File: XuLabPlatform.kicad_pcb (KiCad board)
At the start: 2 copper layers, 134 x 123.5 mm, 73 parts, among them J1 SWD Connector, J10 Servo7, J11 Servo8, J12 Thruster SGN, J13 USB_B_Micro, J14 CAN, J15 I2C, J16 UART, J2 Conn_01x04, J3 1986660-2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

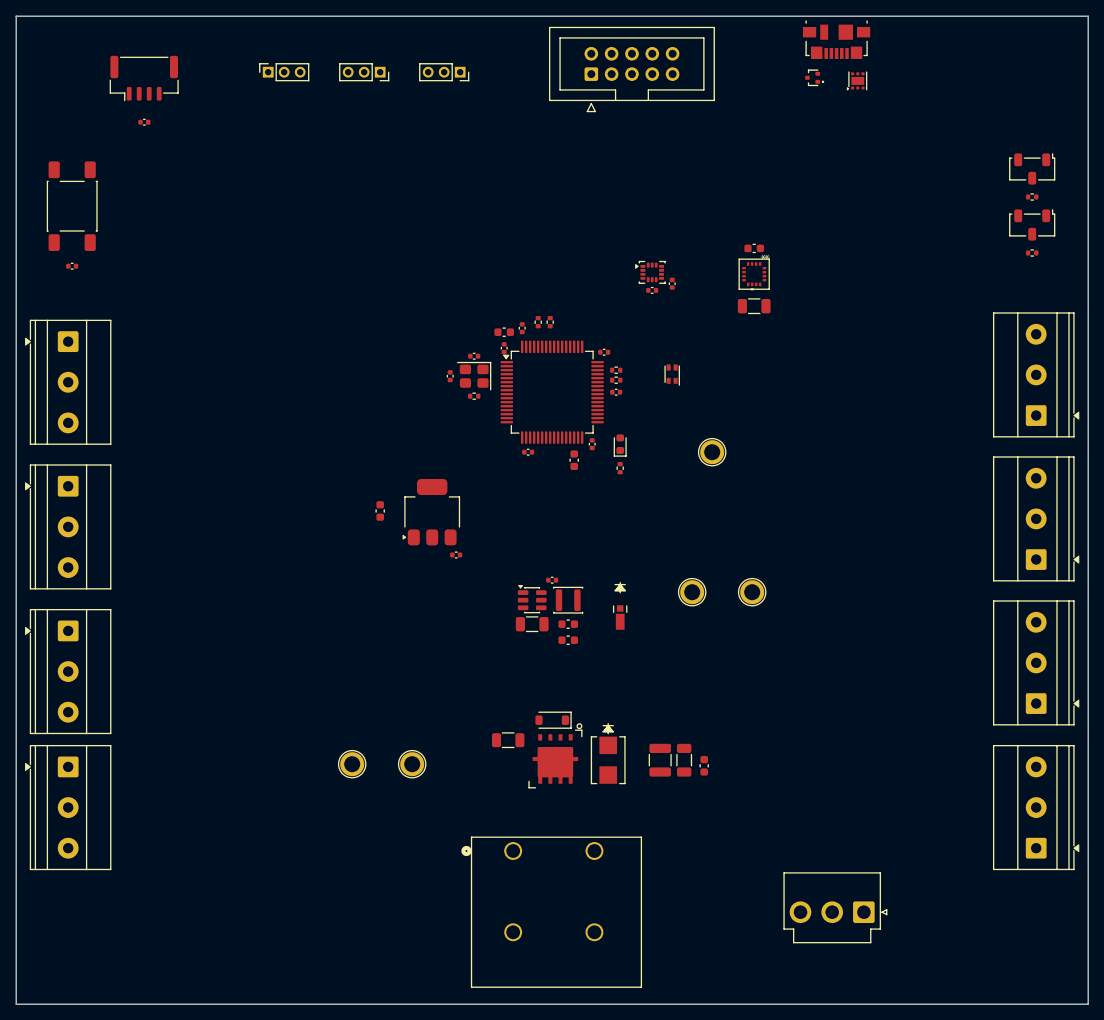
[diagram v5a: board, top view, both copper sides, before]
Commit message: Add ground plane and crystal connections
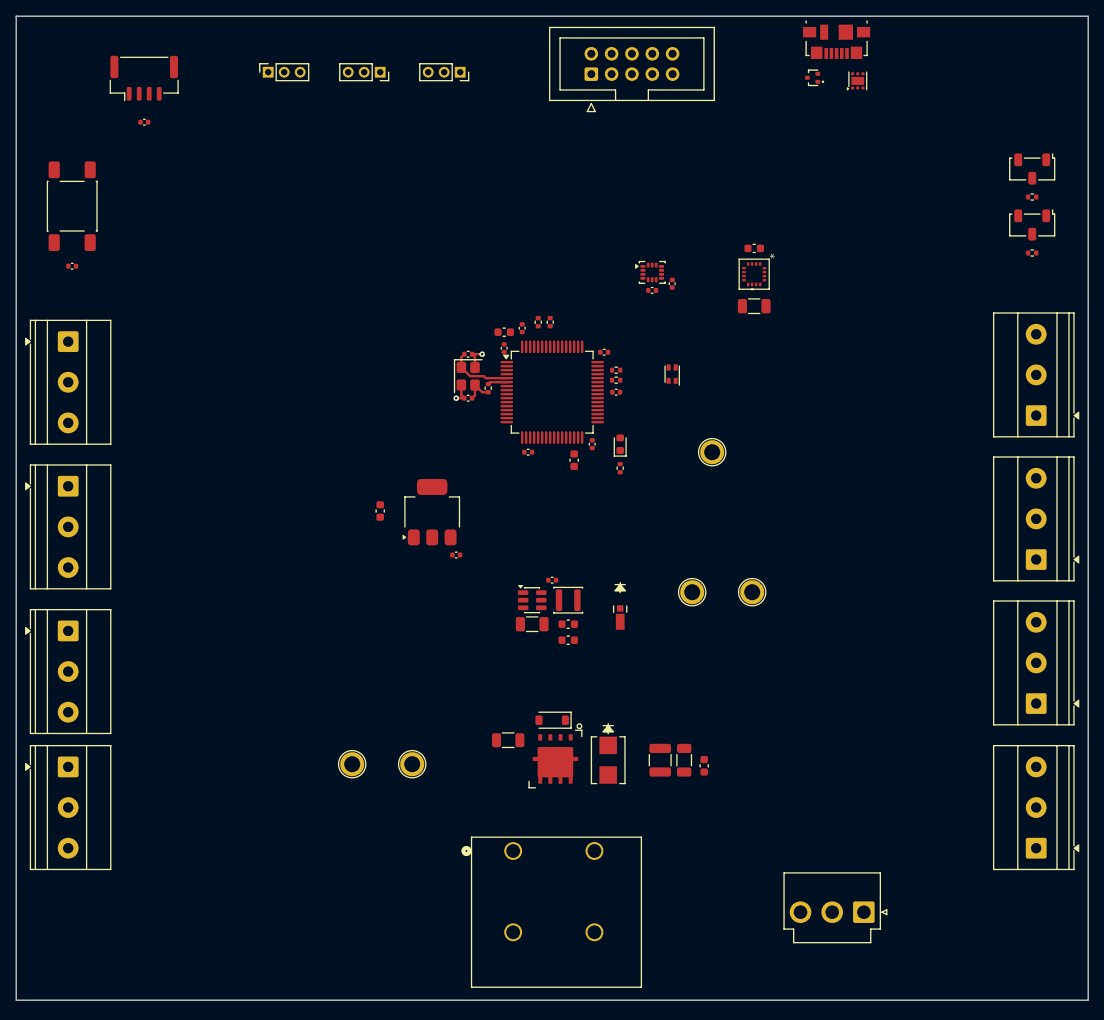
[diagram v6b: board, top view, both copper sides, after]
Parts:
- moved C12 3.55 mm to (139.5, 80.8), turned to 180 degrees
- moved R3 2.02 mm to (142.0, 79.5), turned to -90 degrees
- moved C11 0.79 mm to (139.5, 75.2), turned to 0 degrees
- moved Y1 0.75 mm to (139.5, 78.0), turned to -90 degrees
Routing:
- net /MCU A/RCC_IN: track 0.00 -> 8.04 mm
- net GND: track 0.00 -> 7.15 mm, vias 0 -> 2
- net Net-(C12-Pad1): track 0.00 -> 3.83 mm
- net /MCU A/RCC_OUT: track 0.00 -> 2.42 mm
- added copper zone on In1.Cu, net GND
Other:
- board size 134 x 123.5 mm -> 134 x 123 mm
- copper layers 2 -> 4

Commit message: Add rest of connections
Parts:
- C7, C8, U6: moved to B.Cu
- D2: value 4.7V -> 12V
- R9: value 75 -> 100
- moved SW3 104.5 mm to (105.5, 59.8)
- moved SW2 104.5 mm to (105.5, 52.1)
- moved R1 104.0 mm to (106.0, 55.2)
- moved R2 104.0 mm to (106.0, 62.8)
- moved J12 80.3 mm to (200.2, 65.5), turned to 90 degrees
- moved J4 54.9 mm to (99.5, 72.8)
- moved J7 54.1 mm to (99.5, 126.8)
- moved SW1 40.0 mm to (124.2, 77.5), turned to 180 degrees
- moved C10 30.5 mm to (117.5, 77.5), turned to 90 degrees
- moved J5 21.5 mm to (99.5, 90.8)
- moved J6 19.8 mm to (99.5, 108.8)
- moved R5 17.7 mm to (135.5, 59.0)
- moved R4 17.0 mm to (138.0, 59.0)
- moved CR2 14.5 mm to (144.1, 106.2)
- moved C8 13.8 mm to (142.1, 92.8)
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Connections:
- C13 pad 1: +3V3 -> +3.3V
- C14 pad 1: +3V3 -> +3.3V
- C15 pad 1: +3V3 -> +3.3V
- C17 pad 1: +3V3 -> +3.3V
- D3 pad 1: /MCU A/USB_D_I+ -> /MCU A/USB_D_I-
- D3 pad 2: /MCU A/USB_D_I- -> /MCU A/USB_D_I+
- J10 pad 1: /PWM_7 -> GND
- J10 pad 3: GND -> /PWM_7
- J11 pad 1: /PWM_8 -> GND
- J11 pad 3: GND -> /PWM_8
- J12 pad 1: /PWM_9 -> GND
- J12 pad 3: GND -> /PWM_9
- J15 pad 1: /I2C1_SCL -> /I2C1_SDA
- J15 pad 2: /I2C1_SDA -> /I2C1_SCL
- J16 pad 1: /UART_TX -> /UART_RX
- J16 pad 2: /UART_RX -> /UART_TX
- J2 pad 1: +3V3 -> +3.3V
- J8 pad 1: /PWM_5 -> GND
- J8 pad 3: GND -> /PWM_5
- J9 pad 1: /PWM_6 -> GND
- J9 pad 3: GND -> /PWM_6
- U2 pad 5: +3V3 -> +3.3V
- U2 pad 8: +3V3 -> +3.3V
- U3 pad 13: +3V3 -> +3.3V
- U3 pad 2: +3V3 -> +3.3V
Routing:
- net GND: track 7.15 -> 135.3 mm, vias 2 -> 50
- net /MCU A/NRST: track 0.00 -> 109.9 mm, vias 0 -> 1
- net /I2C1_SCL: track 0.00 -> 82.8 mm
- net /I2C1_SDA: track 0.00 -> 81.7 mm, vias 0 -> 2
- net /PWM_5: track 0.00 -> 77.9 mm
- net /MCU A/USB_VBUS: track 0.00 -> 73.2 mm, vias 0 -> 2
- net /PWM_4: track 0.00 -> 70.1 mm
- net /MCU A/BOOT1: track 0.00 -> 67.4 mm, vias 0 -> 2
- net /PWM_9: track 0.00 -> 63.6 mm
- net /PWM_6: track 0.00 -> 62.8 mm
- net /CAN1_TX: track 0.00 -> 62.4 mm
- net /PWM_8: track 0.00 -> 62.2 mm
- net /CAN1_RX: track 0.00 -> 60.6 mm
- net /MCU A/USB_D_I-: track 0.00 -> 59.2 mm
- net /MCU A/USB_D_I+: track 0.00 -> 58.4 mm
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- added copper zone on F.Cu, net +3.3V
- added copper zone on In2.Cu, net +3.3V
- added copper zone on B.Cu, net +7.4V
- added copper zone on F.Cu, net +7.4V
- added copper zone on In2.Cu, net +7.4V
- added copper zone on F.Cu, net GND
- added copper zone on B.Cu, net Net-(Q2-D)
- added copper zone on F.Cu, net Net-(Q2-D)
- added copper zone on F.Cu, net Net-(U4-SW)
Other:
- board size 134 x 123 mm -> 115 x 123 mm

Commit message: Add silkscreen labels
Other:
- board text added: "+IN"
- board text added: "+X"
- board text added: "+Y"
- board text added: "+Z"
- board text added: "-IN"
- board text added: "3V3"
- board text added: "7V4"
- board text added: "BOOT0"
- board text added: "BOOT1"
- board text added: "CAN"
- board text added: "CLK"
- board text added: "DIO"
- board text added: "GND"
- board text added: "I2C"
- board text added: "LED Output"
- board text added: "PWM"
- board text added: "RST"
- board text added: "RX"
- board text added: "Reset"
- board text added: "SCL"
- board text added: "SDA"
- board text added: "SWO"
- board text added: "Serial Wire Debug"
- board text added: "TX"
- board text added: "UART"
- board text added: "X"
- board text added: "Xu Lab Eval Board Rev. A"
